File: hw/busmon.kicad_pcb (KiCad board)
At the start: 2 copper layers, 24 parts, among them J1 CONN_01X16, J3 DIL14, J4 DIL14, J5 DIL14, J6 DIL14, J7 CONN_01X02, J8 CONN_01X06, Q1 MMBT3906, Q2 MMBT3906, Q3 MMBT3906, Q4 MMBT3906, U1 ATMEGA164A-A

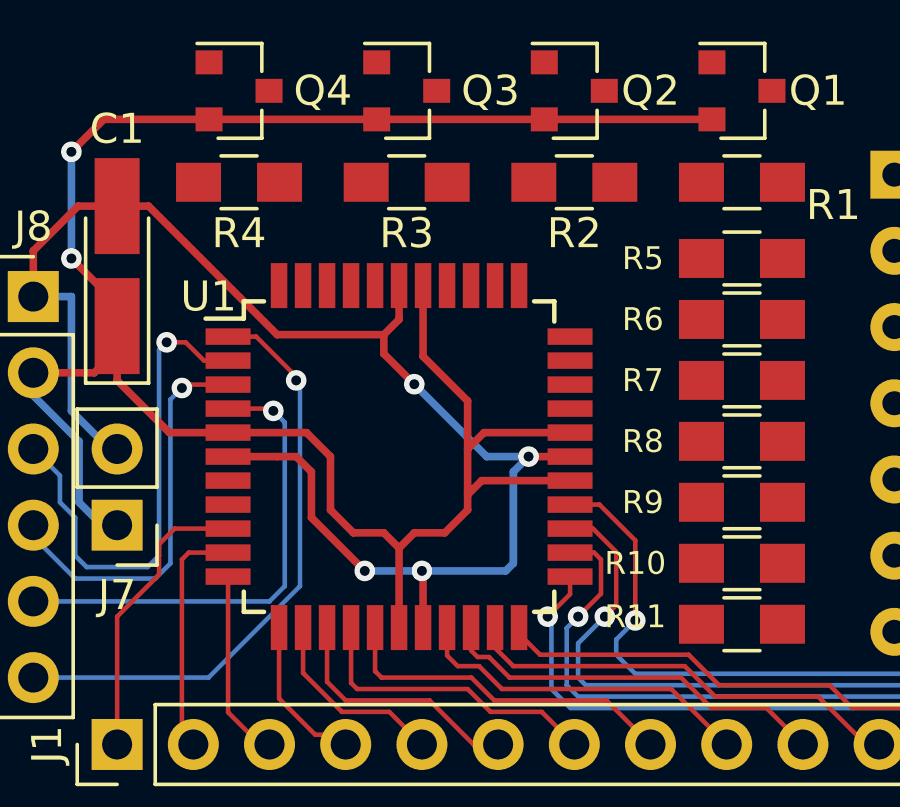
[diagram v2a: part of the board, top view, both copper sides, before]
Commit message: routed more signals
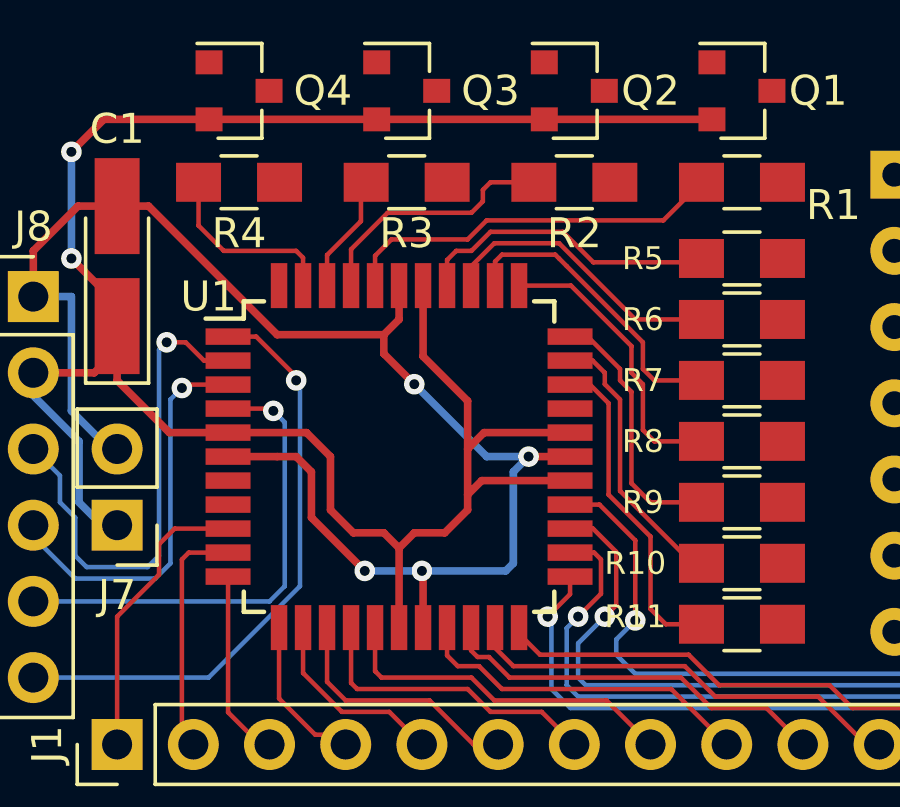
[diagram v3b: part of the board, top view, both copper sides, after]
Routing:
- net Net-(R1-Pad2): track 0.00 -> 12.9 mm
- net Net-(R11-Pad2): track 0.00 -> 10.9 mm
- net Net-(R5-Pad2): track 0.00 -> 10.2 mm
- net Net-(R7-Pad2): track 0.00 -> 10.0 mm
- net Net-(R6-Pad2): track 0.00 -> 9.69 mm
- net Net-(R8-Pad2): track 0.00 -> 9.64 mm
- net Net-(R10-Pad2): track 0.00 -> 9.19 mm
- net Net-(R9-Pad2): track 0.00 -> 8.68 mm
- net Net-(R2-Pad2): track 0.00 -> 8.45 mm
- net Net-(R4-Pad2): track 0.00 -> 6.30 mm
- net Net-(R3-Pad2): track 0.00 -> 3.98 mm
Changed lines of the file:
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@@
   (general
     (links 91)
-    (no_connects 54)
+    (no_connects 43)
     (area 84.347267 79.352599 157.467401 108.128734)
     (thickness 1.6)
     (drawings 0)
-    (tracks 223)
+    (tracks 295)
     (zones 0)
     (modules 24)
@@
   (segment (start 98.171 90.805) (end 98.171 90.932) (width 0.1524) (layer F.Cu) (net 50))
   (segment (start 96.838 89.472) (end 98.171 90.805) (width 0.1524) (layer F.Cu) (net 50))
+  (segment (start 100.8 87.772) (end 100.8 86.779) (width 0.1524) (layer F.Cu) (net 55) (status 400000))
+  (segment (start 110.41 85.598) (end 111.68 84.328) (width 0.1524) (layer F.Cu) (net 55) (status 800000))
+  (segment (start 104.521 85.598) (end 110.41 85.598) (width 0.1524) (layer F.Cu) (net 55))
+  (segment (start 103.886 86.233) (end 104.521 85.598) (width 0.1524) (layer F.Cu) (net 55))
+  (segment (start 101.346 86.233) (end 103.886 86.233) (width 0.1524) (layer F.Cu) (net 55))
+  (segment (start 100.8 86.779) (end 101.346 86.233) (width 0.1524) (layer F.Cu) (net 55))
+  (segment (start 100 87.772) (end 100 86.563) (width 0.1524) (layer F.Cu) (net 56) (status 400000))
+  (segment (start 104.648 84.328) (end 106.092 84.328) (width 0.1524) (layer F.Cu) (net 56) (status 800000))
+  (segment (start 104.394 84.582) (end 104.648 84.328) (width 0.1524) (layer F.Cu) (net 56))
+  (segment (start 104.394 84.963) (end 104.394 84.582) (width 0.1524) (layer F.Cu) (net 56))
+  (segment (start 104.013 85.344) (end 104.394 84.963) (width 0.1524) (layer F.Cu) (net 56))
+  (segment (start 101.219 85.344) (end 104.013 85.344) (width 0.1524) (layer F.Cu) (net 56))
+  (segment (start 100 86.563) (end 101.219 85.344) (width 0.1524) (layer F.Cu) (net 56))
+  (segment (start 99.2 87.772) (end 99.2 86.754) (width 0.1524) (layer F.Cu) (net 57) (status 400000))
+  (segment (start 100.33 85.624) (end 100.33 84.502) (width 0.1524) (layer F.Cu) (net 57) (status 800000))
+  (segment (start 99.2 86.754) (end 100.33 85.624) (width 0.1524) (layer F.Cu) (net 57))
+  (segment (start 100.33 84.502) (end 100.504 84.328) (width 0.1524) (layer F.Cu) (net 57) (status C00000))
+  (segment (start 98.4 87.772) (end 98.4 86.843) (width 0.1524) (layer F.Cu) (net 58) (status 400000))
+  (segment (start 94.916 85.772) (end 94.916 84.328) (width 0.1524) (layer F.Cu) (net 58) (status 800000))
+  (segment (start 95.758 86.614) (end 94.916 85.772) (width 0.1524) (layer F.Cu) (net 58))
+  (segment (start 98.171 86.614) (end 95.758 86.614) (width 0.1524) (layer F.Cu) (net 58))
+  (segment (start 98.4 86.843) (end 98.171 86.614) (width 0.1524) (layer F.Cu) (net 58))
+  (segment (start 103.2 87.772) (end 103.2 86.919) (width 0.1524) (layer F.Cu) (net 59) (status 400000))
+  (segment (start 108.077 86.995) (end 111.553 86.995) (width 0.1524) (layer F.Cu) (net 59) (status 800000))
+  (segment (start 107.061 85.979) (end 108.077 86.995) (width 0.1524) (layer F.Cu) (net 59))
+  (segment (start 104.648 85.979) (end 107.061 85.979) (width 0.1524) (layer F.Cu) (net 59))
+  (segment (start 104.013 86.614) (end 104.648 85.979) (width 0.1524) (layer F.Cu) (net 59))
+  (segment (start 103.505 86.614) (end 104.013 86.614) (width 0.1524) (layer F.Cu) (net 59))
+  (segment (start 103.2 86.919) (end 103.505 86.614) (width 0.1524) (layer F.Cu) (net 59))
+  (segment (start 111.553 86.995) (end 111.68 86.868) (width 0.1524) (layer F.Cu) (net 59) (status C00000))
+  (segment (start 104 87.772) (end 104 87.135) (width 0.1524) (layer F.Cu) (net 60) (status C00000))
+  (segment (start 104 87.135) (end 104.775 86.36) (width 0.1524) (layer F.Cu) (net 60) (status 400000))
+  (segment (start 104.775 86.36) (end 106.934 86.36) (width 0.1524) (layer F.Cu) (net 60))
+  (segment (start 106.934 86.36) (end 109.474 88.9) (width 0.1524) (layer F.Cu) (net 60))
+  (segment (start 109.474 88.9) (end 111.68 88.9) (width 0.1524) (layer F.Cu) (net 60) (status 800000))
+  (segment (start 104.8 87.772) (end 104.8 86.97) (width 0.1524) (layer F.Cu) (net 61) (status 400000))
+  (segment (start 110.109 90.932) (end 111.68 90.932) (width 0.1524) (layer F.Cu) (net 61) (status 800000))
+  (segment (start 109.728 90.551) (end 110.109 90.932) (width 0.1524) (layer F.Cu) (net 61))
+  (segment (start 109.728 89.662) (end 109.728 90.551) (width 0.1524) (layer F.Cu) (net 61))
+  (segment (start 107.188 87.122) (end 109.728 89.662) (width 0.1524) (layer F.Cu) (net 61))
+  (segment (start 106.934 86.868) (end 107.188 87.122) (width 0.1524) (layer F.Cu) (net 61))
+  (segment (start 106.807 86.741) (end 106.934 86.868) (width 0.1524) (layer F.Cu) (net 61))
+  (segment (start 105.029 86.741) (end 106.807 86.741) (width 0.1524) (layer F.Cu) (net 61))
+  (segment (start 104.8 86.97) (end 105.029 86.741) (width 0.1524) (layer F.Cu) (net 61))
+  (segment (start 105.6 87.772) (end 107.33 87.772) (width 0.1524) (layer F.Cu) (net 62) (status 400000))
+  (segment (start 110.109 92.964) (end 111.68 92.964) (width 0.1524) (layer F.Cu) (net 62) (status 800000))
+  (segment (start 109.728 92.583) (end 110.109 92.964) (width 0.1524) (layer F.Cu) (net 62))
+  (segment (start 109.728 91.059) (end 109.728 92.583) (width 0.1524) (layer F.Cu) (net 62))
+  (segment (start 109.347 90.678) (end 109.728 91.059) (width 0.1524) (layer F.Cu) (net 62))
+  (segment (start 109.347 89.789) (end 109.347 90.678) (width 0.1524) (layer F.Cu) (net 62))
+  (segment (start 107.33 87.772) (end 109.347 89.789) (width 0.1524) (layer F.Cu) (net 62))
+  (segment (start 107.3 89.472) (end 107.887 89.472) (width 0.1524) (layer F.Cu) (net 63) (status C00000))
+  (segment (start 107.887 89.472) (end 108.966 90.551) (width 0.1524) (layer F.Cu) (net 63) (status 400000))
+  (segment (start 108.966 90.551) (end 108.966 90.932) (width 0.1524) (layer F.Cu) (net 63))
+  (segment (start 108.966 90.932) (end 109.347 91.313) (width 0.1524) (layer F.Cu) (net 63))
+  (segment (start 109.347 91.313) (end 109.347 94.361) (width 0.1524) (layer F.Cu) (net 63))
+  (segment (start 109.347 94.361) (end 109.982 94.996) (width 0.1524) (layer F.Cu) (net 63))
+  (segment (start 109.982 94.996) (end 111.68 94.996) (width 0.1524) (layer F.Cu) (net 63) (status 800000))
+  (segment (start 107.3 90.272) (end 108.052 90.272) (width 0.1524) (layer F.Cu) (net 64) (status 400000))
+  (segment (start 108.966 94.615) (end 111.379 97.028) (width 0.1524) (layer F.Cu) (net 64) (status 800000))
+  (segment (start 108.966 91.567) (end 108.966 94.615) (width 0.1524) (layer F.Cu) (net 64))
+  (segment (start 108.458 91.059) (end 108.966 91.567) (width 0.1524) (layer F.Cu) (net 64))
+  (segment (start 108.458 90.678) (end 108.458 91.059) (width 0.1524) (layer F.Cu) (net 64))
+  (segment (start 108.052 90.272) (end 108.458 90.678) (width 0.1524) (layer F.Cu) (net 64))
+  (segment (start 111.379 97.028) (end 111.68 97.028) (width 0.1524) (layer F.Cu) (net 64) (status C00000))
+  (segment (start 107.3 91.072) (end 107.963 91.072) (width 0.1524) (layer F.Cu) (net 65) (status C00000))
+  (segment (start 107.963 91.072) (end 108.585 91.694) (width 0.1524) (layer F.Cu) (net 65) (status 400000))
+  (segment (start 108.585 91.694) (end 108.585 94.742) (width 0.1524) (layer F.Cu) (net 65))
+  (segment (start 108.585 94.742) (end 109.982 96.139) (width 0.1524) (layer F.Cu) (net 65))
+  (segment (start 109.982 96.139) (end 109.982 98.552) (width 0.1524) (layer F.Cu) (net 65))
+  (segment (start 109.982 98.552) (end 110.49 99.06) (width 0.1524) (layer F.Cu) (net 65))
+  (segment (start 110.49 99.06) (end 111.68 99.06) (width 0.1524) (layer F.Cu) (net 65) (status 800000))
 )

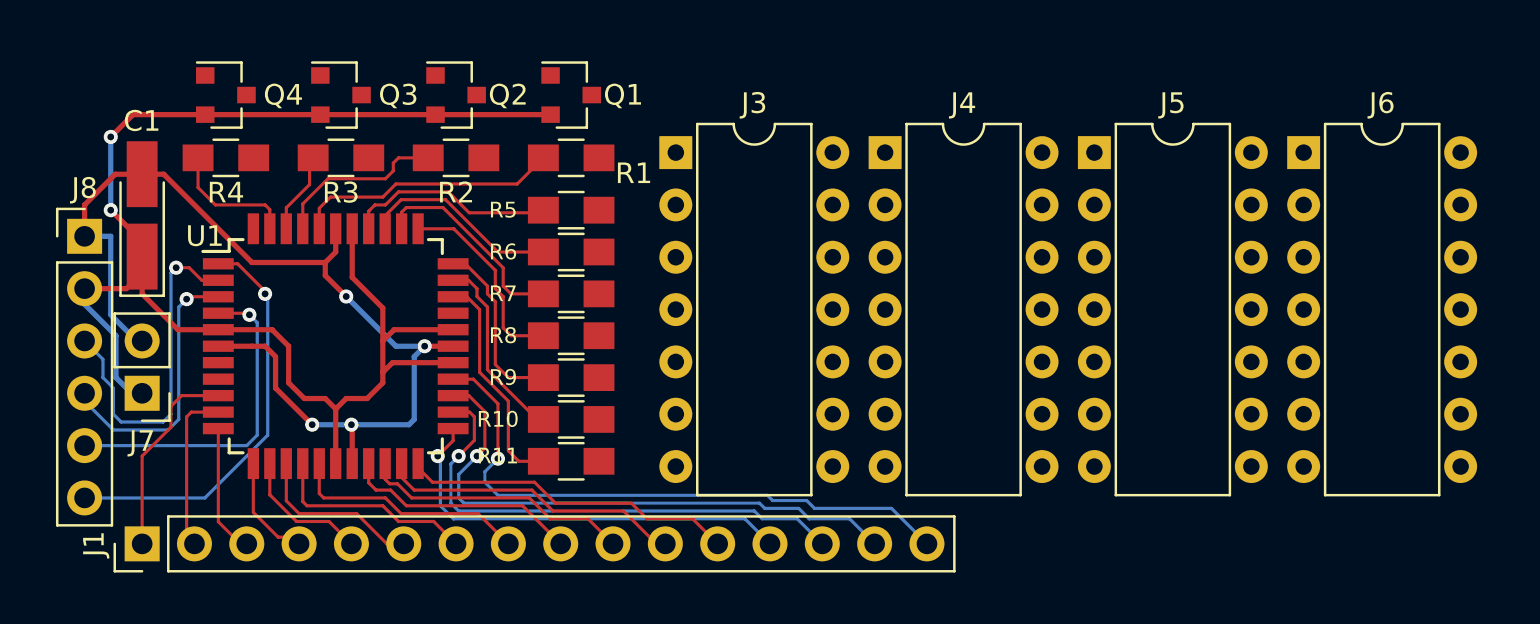
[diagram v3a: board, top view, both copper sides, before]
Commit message: routed all signals
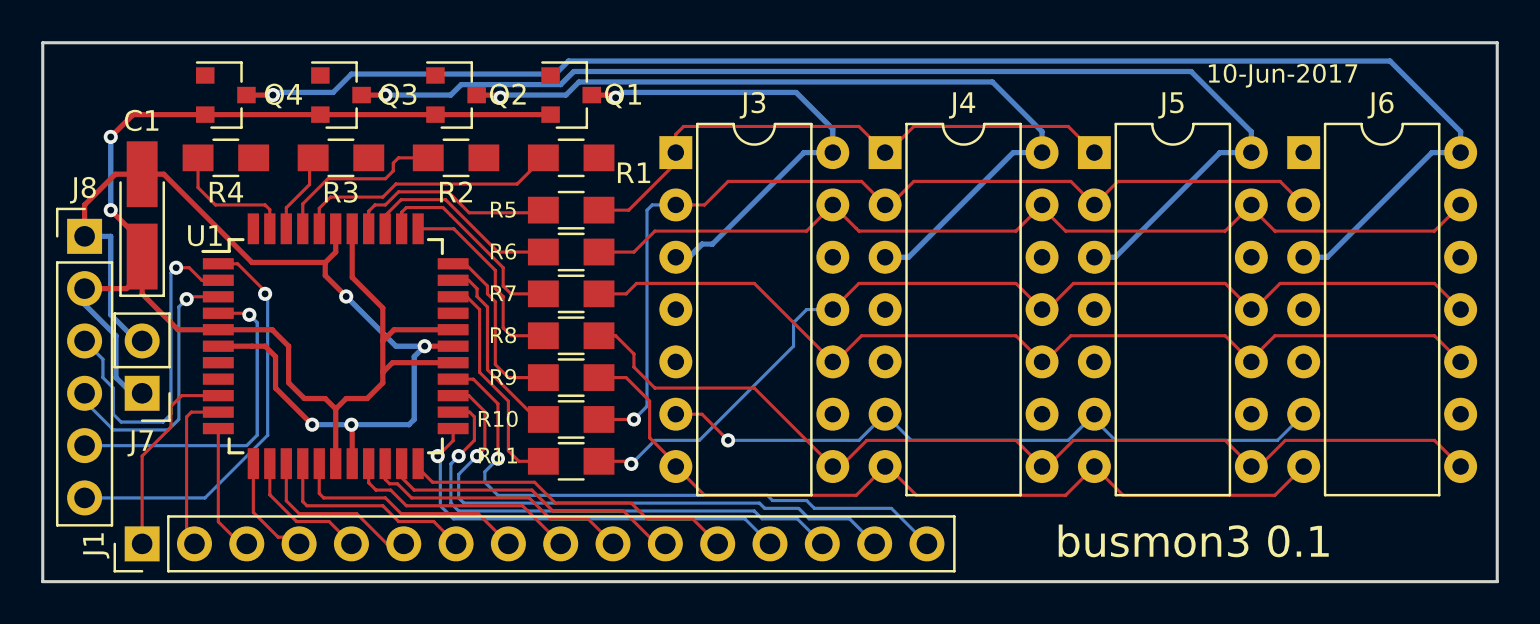
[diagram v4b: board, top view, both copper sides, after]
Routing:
- net /CA4: track 0.00 -> 71.8 mm, vias 0 -> 1
- net /CA3: track 0.00 -> 55.6 mm, vias 0 -> 1
- net /G: track 0.00 -> 48.8 mm, vias 0 -> 1
- net /D: track 0.00 -> 48.0 mm
- net /F: track 0.00 -> 46.9 mm, vias 0 -> 1
- net /C: track 0.00 -> 46.8 mm
- net /B: track 0.00 -> 46.1 mm
- net /E: track 0.00 -> 40.6 mm
- net /CA2: track 0.00 -> 39.6 mm, vias 0 -> 1
- net /DP: track 0.00 -> 33.8 mm, vias 0 -> 1
- net /A: track 0.00 -> 28.1 mm
- net /CA1: track 0.00 -> 24.4 mm, vias 0 -> 1
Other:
- board outline added: 70.6 x 26.2 mm
- board text added: "10-Jun-2017"
- board text added: "busmon3 0.1"

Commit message: routed a few missed signals
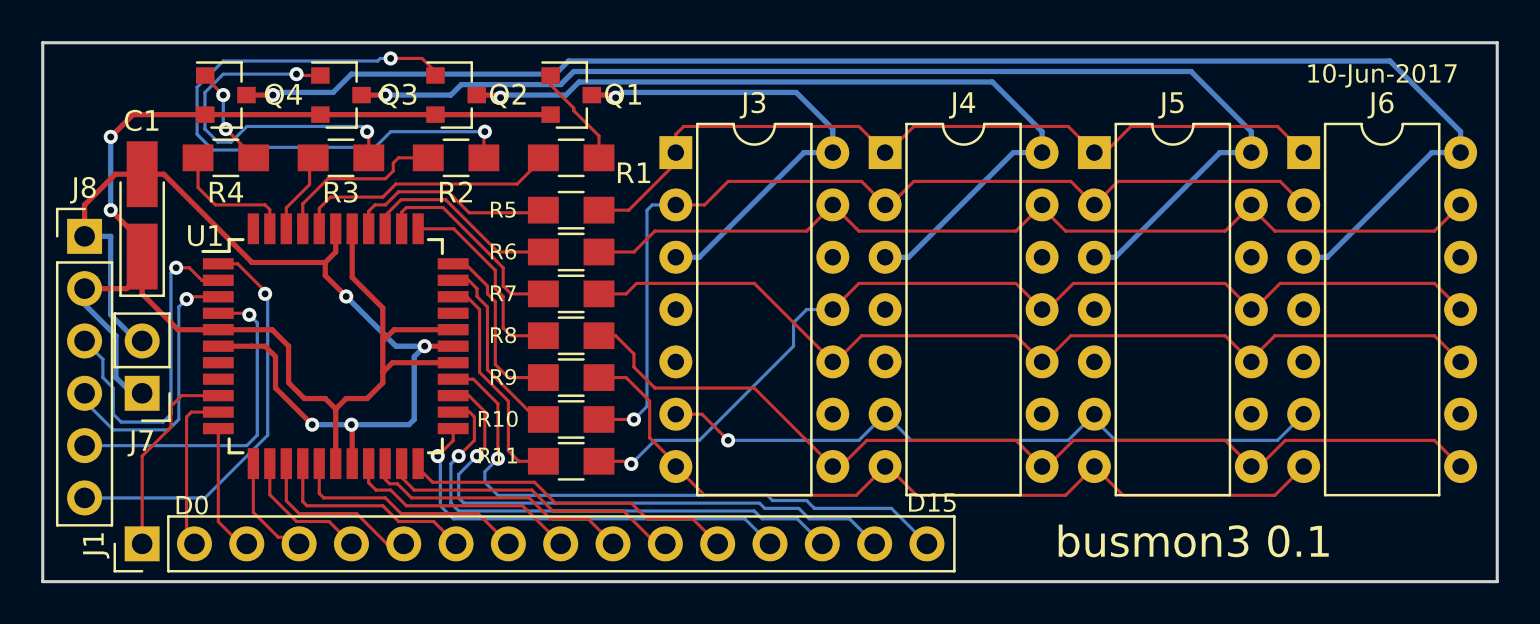
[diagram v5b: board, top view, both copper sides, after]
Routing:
- net Net-(Q2-Pad1): track 0.00 -> 30.8 mm, vias 0 -> 2
- net Net-(Q3-Pad1): track 0.00 -> 17.6 mm, vias 0 -> 2
- net /A: track 28.1 -> 39.3 mm
- net Net-(Q4-Pad1): track 0.00 -> 4.97 mm, vias 0 -> 2
- net Net-(Q1-Pad1): track 0.00 -> 4.97 mm
- net /CA1: track 24.4 -> 23.5 mm
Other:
- board text added: "D0"
- board text added: "D15"

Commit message: improve schematic, minor silkscreen fixes
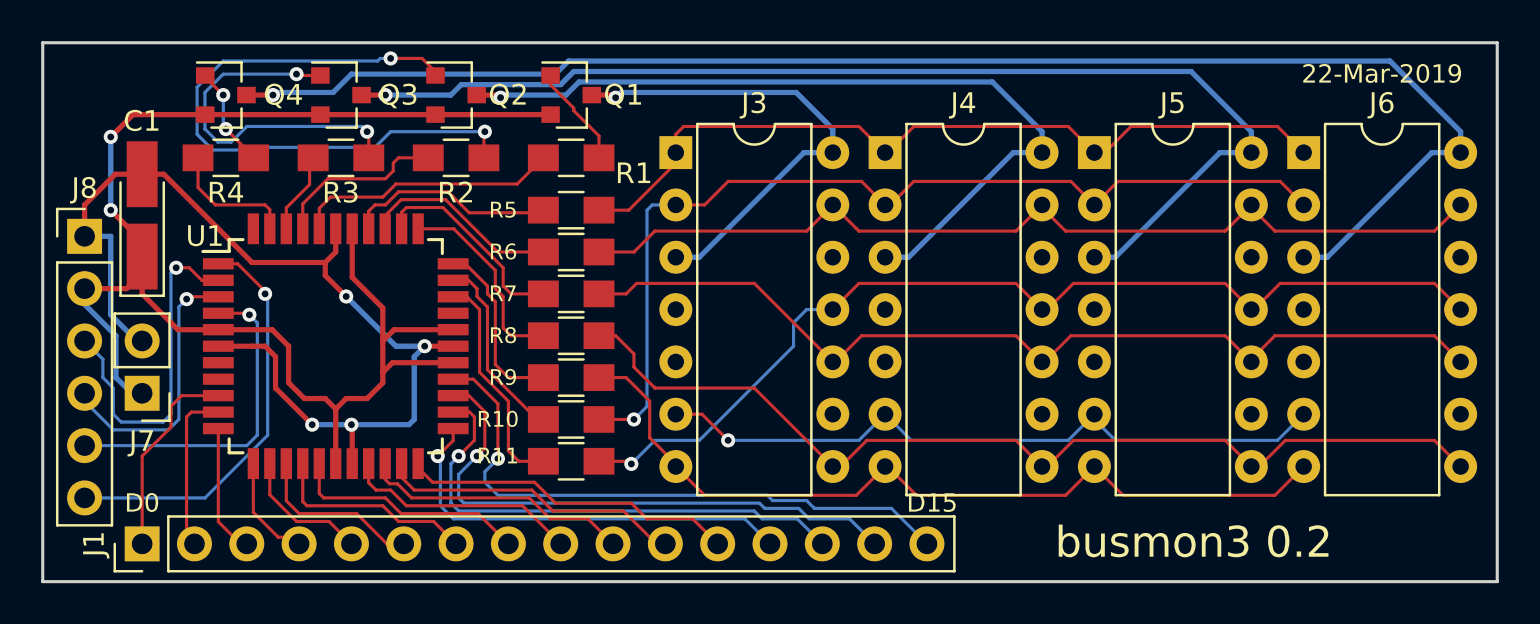
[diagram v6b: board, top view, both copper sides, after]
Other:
- board text added: "22-Mar-2019"
- board text added: "busmon3 0.2"
- board text removed: "10-Jun-2017"
- board text removed: "busmon3 0.1"
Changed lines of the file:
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@@
-(kicad_pcb (version 4) (host pcbnew 4.0.2+e4-6225~38~ubuntu14.04.1-stable)
+(kicad_pcb (version 20171130) (host pcbnew 5.0.2-bee76a0~70~ubuntu16.04.1)
   (general
-    (links 91)
-    (no_connects 0)
-    (area 84.347267 78.664999 158.063001 108.128734)
     (thickness 1.6)
     (drawings 8)
@@
     (pad_drill 0.762)
     (pad_to_mask_clearance 0.2)
+    (solder_mask_min_width 0.25)
     (aux_axis_origin 0 0)
     (visible_elements FFFFFF7F)
@@
       (layerselection 0x00030_80000001)
       (usegerberextensions false)
+      (usegerberattributes false)
+      (usegerberadvancedattributes false)
+      (creategerberjobfile false)
       (excludeedgelayer true)
       (linewidth 0.100000)
@@
       (hpglpennumber 1)
       (hpglpenspeed 20)
-      (hpglpendiameter 15)
-      (hpglpenoverlay 2)
+      (hpglpendiameter 15.000000)
       (psnegative false)
       (psa4output false)
@@
       (net 18 /D15))
     (model ${KISYS3DMOD}/Pin_Headers.3dshapes/Pin_Header_Straight_1x16_Pitch2.54mm.wrl
-      (at (xyz 0 -0.75 0))
+      (offset (xyz 0 -19.04999971389771 0))
       (scale (xyz 1 1 1))
       (rotate (xyz 0 0 90))
@@
       (net 2 GND))
     (model ${KISYS3DMOD}/Pin_Headers.3dshapes/Pin_Header_Straight_1x02_Pitch2.54mm.wrl
-      (at (xyz 0 -0.05 0))
+      (offset (xyz 0 -1.269999980926514 0))
       (scale (xyz 1 1 1))
       (rotate (xyz 0 0 90))
@@
       (net 50 "Net-(J8-Pad6)"))
     (model ${KISYS3DMOD}/Pin_Headers.3dshapes/Pin_Header_Straight_1x06_Pitch2.54mm.wrl
-      (at (xyz 0 -0.25 0))
+      (offset (xyz 0 -6.349999904632568 0))
       (scale (xyz 1 1 1))
       (rotate (xyz 0 0 90))
@@
     (effects (font (size 0.889 0.889) (thickness 0.22225)))
   )
-  (gr_text D0 (at 94.615 101.219) (layer F.SilkS)
+  (gr_text D0 (at 92.202 101.092) (layer F.SilkS)
     (effects (font (size 0.889 0.889) (thickness 0.22225)))
   )
@@
   (gr_line (start 87.376 78.74) (end 87.376 104.902) (angle 90) (layer Edge.Cuts) (width 0.15))
   (gr_line (start 157.988 78.74) (end 87.376 78.74) (angle 90) (layer Edge.Cuts) (width 0.15))
-  (gr_text 10-Jun-2017 (at 152.4 80.264) (layer F.SilkS)
+  (gr_text 22-Mar-2019 (at 152.4 80.264) (layer F.SilkS)
     (effects (font (size 0.889 0.889) (thickness 0.22225)))
   )
-  (gr_text "busmon3 0.1" (at 143.256 102.997) (layer F.SilkS)
+  (gr_text "busmon3 0.2" (at 143.256 102.997) (layer F.SilkS)
     (effects (font (size 1.5 1.5) (thickness 0.3)))
   )
